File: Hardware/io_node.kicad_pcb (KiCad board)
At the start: 2 copper layers, 50 x 100 mm, 18 parts, among them U1 STM32F405RGT6, Y1 8 MHz

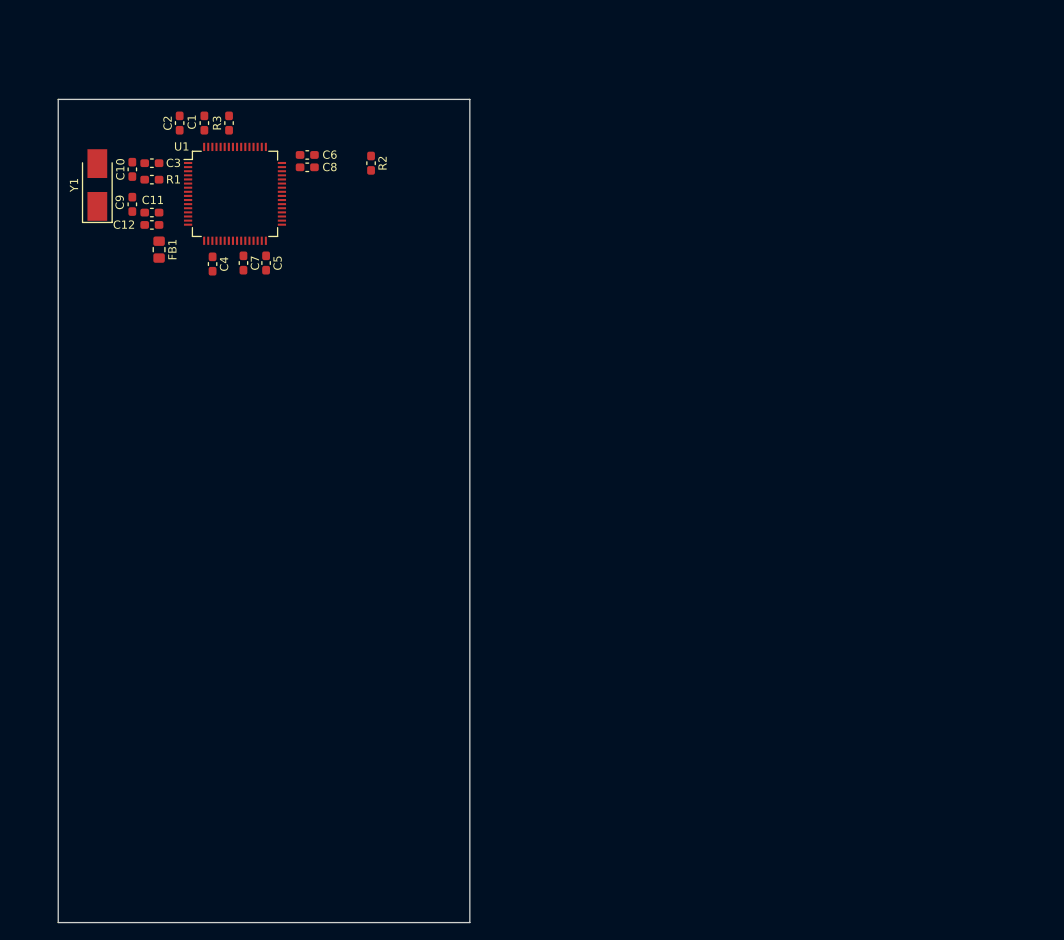
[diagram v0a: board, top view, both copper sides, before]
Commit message: Add in and output drivers
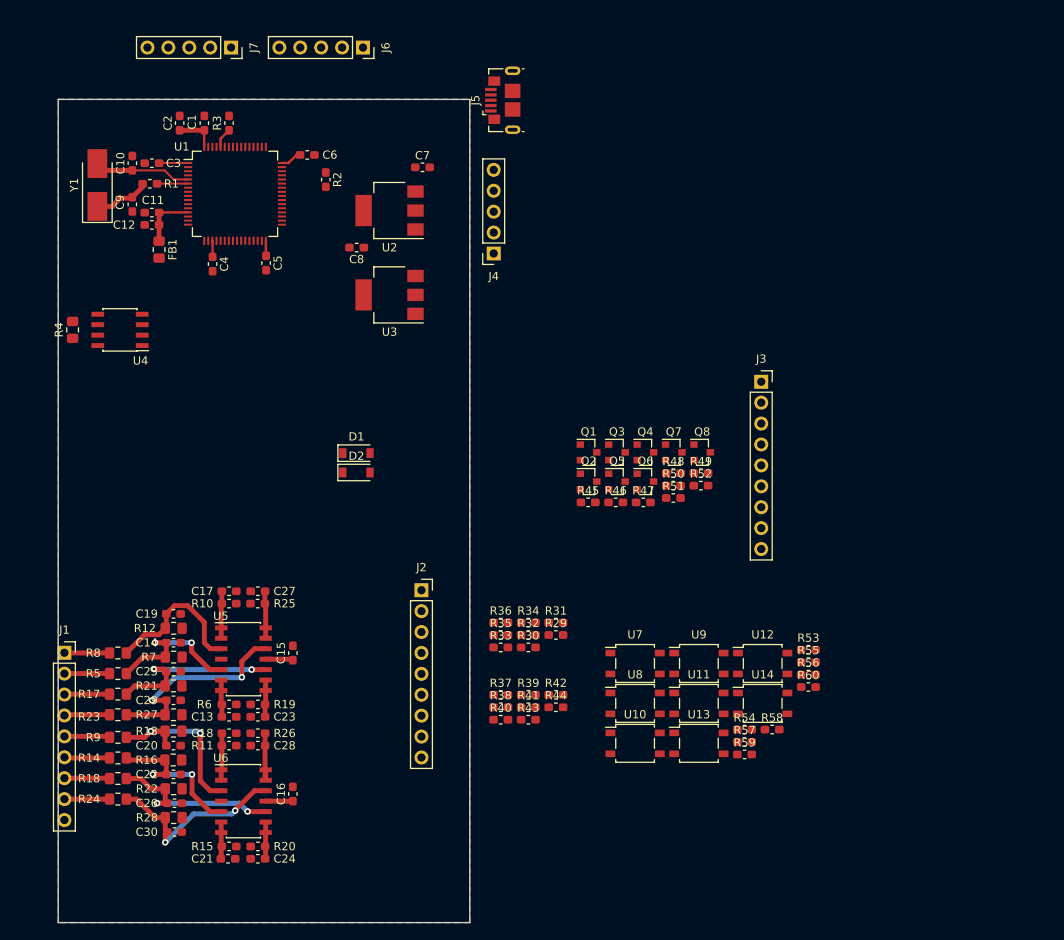
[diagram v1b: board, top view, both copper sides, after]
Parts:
- added C13: 1NF, Capacitor_SMD:C_0603_1608Metric_Pad1.05x0.95mm_HandSolder, F.Cu at (70.8, 100.0)
- added C14: 100NF, Capacitor_SMD:C_0603_1608Metric_Pad1.05x0.95mm_HandSolder, F.Cu at (64.0, 91.0)
- added C15: 100NF, Capacitor_SMD:C_0603_1608Metric_Pad1.05x0.95mm_HandSolder, F.Cu at (78.5, 92.2)
- added C16: 100NF, Capacitor_SMD:C_0603_1608Metric_Pad1.05x0.95mm_HandSolder, F.Cu at (78.5, 109.4)
- added C17: 1NF, Capacitor_SMD:C_0603_1608Metric_Pad1.05x0.95mm_HandSolder, F.Cu at (70.8, 84.8)
- added C18: 1NF, Capacitor_SMD:C_0603_1608Metric_Pad1.05x0.95mm_HandSolder, F.Cu at (70.8, 102.0)
- added C19: 100NF, Capacitor_SMD:C_0603_1608Metric_Pad1.05x0.95mm_HandSolder, F.Cu at (64.0, 87.5)
- added C20: 100NF, Capacitor_SMD:C_0603_1608Metric_Pad1.05x0.95mm_HandSolder, F.Cu at (64.0, 103.5)
- added C21: 1NF, Capacitor_SMD:C_0603_1608Metric_Pad1.05x0.95mm_HandSolder, F.Cu at (70.6, 117.2)
- added C22: 100NF, Capacitor_SMD:C_0603_1608Metric_Pad1.05x0.95mm_HandSolder, F.Cu at (64.0, 107.0)
- added C23: 1NF, Capacitor_SMD:C_0603_1608Metric_Pad1.05x0.95mm_HandSolder, F.Cu at (74.2, 100.0)
- added C24: 1NF, Capacitor_SMD:C_0603_1608Metric_Pad1.05x0.95mm_HandSolder, F.Cu at (74.2, 117.2)
- added C25: 100NF, Capacitor_SMD:C_0603_1608Metric_Pad1.05x0.95mm_HandSolder, F.Cu at (64.0, 94.5)
- added C26: 100NF, Capacitor_SMD:C_0603_1608Metric_Pad1.05x0.95mm_HandSolder, F.Cu at (64.1, 110.5)
- added C27: 1NF, Capacitor_SMD:C_0603_1608Metric_Pad1.05x0.95mm_HandSolder, F.Cu at (74.2, 84.8)
- added C28: 1NF, Capacitor_SMD:C_0603_1608Metric_Pad1.05x0.95mm_HandSolder, F.Cu at (74.2, 103.5)
- added C29: 100NF, Capacitor_SMD:C_0603_1608Metric_Pad1.05x0.95mm_HandSolder, F.Cu at (64.0, 98.0)
- added C30: 100NF, Capacitor_SMD:C_0603_1608Metric_Pad1.05x0.95mm_HandSolder, F.Cu at (64.1, 114.0)
- added D1: B5819W, Diode_SMD:D_SOD-123, F.Cu at (86.2, 68.0)
- added D2: B5819W, Diode_SMD:D_SOD-123, F.Cu at (86.2, 70.3)
- added J1: Conn_01x09, Connector_PinSocket_2.54mm:PinSocket_1x09_P2.54mm_Vertical, F.Cu at (50.8, 92.2)
- added J2: Conn_01x09, Connector_PinSocket_2.54mm:PinSocket_1x09_P2.54mm_Vertical, F.Cu at (94.1, 84.6)
- added J3: Conn_01x09, Connector_PinSocket_2.54mm:PinSocket_1x09_P2.54mm_Vertical, F.Cu at (135.4, 59.3)
- added J4: Conn_01x05, Connector_PinSocket_2.54mm:PinSocket_1x05_P2.54mm_Vertical, F.Cu at (102.9, 43.7)
- added J5: USB_B_Micro, Connector_USB:USB_Micro-B_GCT_USB3076-30-A, F.Cu at (104.0, 25.1)
- added J6: Conn_01x05, Connector_PinSocket_2.54mm:PinSocket_1x05_P2.54mm_Vertical, F.Cu at (87.0, 18.7)
- added J7: Conn_01x05, Connector_PinSocket_2.54mm:PinSocket_1x05_P2.54mm_Vertical, F.Cu at (71.0, 18.7)
- added Q1: 2N7002, Package_TO_SOT_SMD:SOT-23, F.Cu at (114.4, 67.9)
- added Q2: 2N7002, Package_TO_SOT_SMD:SOT-23, F.Cu at (114.4, 71.4)
- added Q3: 2N7002, Package_TO_SOT_SMD:SOT-23, F.Cu at (117.9, 67.9)
- added Q4: 2N7002, Package_TO_SOT_SMD:SOT-23, F.Cu at (121.3, 67.9)
- added Q5: 2N7002, Package_TO_SOT_SMD:SOT-23, F.Cu at (117.9, 71.4)
- added Q6: 2N7002, Package_TO_SOT_SMD:SOT-23, F.Cu at (121.3, 71.4)
- added Q7: 2N7002, Package_TO_SOT_SMD:SOT-23, F.Cu at (124.8, 67.9)
- added Q8: 2N7002, Package_TO_SOT_SMD:SOT-23, F.Cu at (128.2, 67.9)
- added R10: 10K, Resistor_SMD:R_0603_1608Metric_Pad1.05x0.95mm_HandSolder, F.Cu at (70.8, 86.2)
- added R11: 10K, Resistor_SMD:R_0603_1608Metric_Pad1.05x0.95mm_HandSolder, F.Cu at (70.8, 103.5)
- added R12: 10K, Resistor_SMD:R_0805_2012Metric_Pad1.15x1.40mm_HandSolder, F.Cu at (64.0, 89.2)
- added R13: 10K, Resistor_SMD:R_0805_2012Metric_Pad1.15x1.40mm_HandSolder, F.Cu at (64.0, 101.8)
- added R14: 150K, Resistor_SMD:R_0805_2012Metric_Pad1.15x1.40mm_HandSolder, F.Cu at (57.2, 105.0)
- added R15: 10K, Resistor_SMD:R_0603_1608Metric_Pad1.05x0.95mm_HandSolder, F.Cu at (70.8, 115.8)
- added R16: 10K, Resistor_SMD:R_0805_2012Metric_Pad1.15x1.40mm_HandSolder, F.Cu at (64.0, 105.2)
- added R17: 150K, Resistor_SMD:R_0805_2012Metric_Pad1.15x1.40mm_HandSolder, F.Cu at (57.2, 97.2)
- added R18: 150K, Resistor_SMD:R_0805_2012Metric_Pad1.15x1.40mm_HandSolder, F.Cu at (57.2, 107.5)
- added R19: 10K, Resistor_SMD:R_0603_1608Metric_Pad1.05x0.95mm_HandSolder, F.Cu at (74.2, 98.5)
- added R20: 10K, Resistor_SMD:R_0603_1608Metric_Pad1.05x0.95mm_HandSolder, F.Cu at (74.2, 115.8)
- added R21: 10K, Resistor_SMD:R_0805_2012Metric_Pad1.15x1.40mm_HandSolder, F.Cu at (64.0, 96.2)
- added R22: 10K, Resistor_SMD:R_0805_2012Metric_Pad1.15x1.40mm_HandSolder, F.Cu at (64.0, 108.8)
- added R23: 150K, Resistor_SMD:R_0805_2012Metric_Pad1.15x1.40mm_HandSolder, F.Cu at (57.2, 99.8)
- added R24: 150K, Resistor_SMD:R_0805_2012Metric_Pad1.15x1.40mm_HandSolder, F.Cu at (57.2, 110.0)
- added R25: 10K, Resistor_SMD:R_0603_1608Metric_Pad1.05x0.95mm_HandSolder, F.Cu at (74.2, 86.2)
- added R26: 10K, Resistor_SMD:R_0603_1608Metric_Pad1.05x0.95mm_HandSolder, F.Cu at (74.2, 102.0)
- added R27: 10K, Resistor_SMD:R_0805_2012Metric_Pad1.15x1.40mm_HandSolder, F.Cu at (64.0, 99.8)
- added R28: 10K, Resistor_SMD:R_0805_2012Metric_Pad1.15x1.40mm_HandSolder, F.Cu at (64.0, 112.2)
- added R29: 10K, Resistor_SMD:R_0603_1608Metric_Pad1.05x0.95mm_HandSolder, F.Cu at (110.5, 90.1)
- added R30: 10K, Resistor_SMD:R_0603_1608Metric_Pad1.05x0.95mm_HandSolder, F.Cu at (107.1, 91.6)
- added R31: 470R, Resistor_SMD:R_0603_1608Metric_Pad1.05x0.95mm_HandSolder, F.Cu at (110.5, 88.6)
- added R32: 470R, Resistor_SMD:R_0603_1608Metric_Pad1.05x0.95mm_HandSolder, F.Cu at (107.1, 90.1)
- added R33: 10K, Resistor_SMD:R_0603_1608Metric_Pad1.05x0.95mm_HandSolder, F.Cu at (103.8, 91.6)
- added R34: 10K, Resistor_SMD:R_0603_1608Metric_Pad1.05x0.95mm_HandSolder, F.Cu at (107.1, 88.6)
- added R35: 470R, Resistor_SMD:R_0603_1608Metric_Pad1.05x0.95mm_HandSolder, F.Cu at (103.8, 90.1)
- added R36: 470R, Resistor_SMD:R_0603_1608Metric_Pad1.05x0.95mm_HandSolder, F.Cu at (103.8, 88.6)
- added R37: 1K, Resistor_SMD:R_0603_1608Metric_Pad1.05x0.95mm_HandSolder, F.Cu at (103.8, 97.3)
- added R38: 10K, Resistor_SMD:R_0603_1608Metric_Pad1.05x0.95mm_HandSolder, F.Cu at (103.8, 98.8)
- added R39: 1K, Resistor_SMD:R_0603_1608Metric_Pad1.05x0.95mm_HandSolder, F.Cu at (107.1, 97.3)
- added R4: 120R, Resistor_SMD:R_0805_2012Metric_Pad1.15x1.40mm_HandSolder, F.Cu at (51.8, 53.0)
- added R40: 10K, Resistor_SMD:R_0603_1608Metric_Pad1.05x0.95mm_HandSolder, F.Cu at (103.8, 100.4)
- added R41: 1K, Resistor_SMD:R_0603_1608Metric_Pad1.05x0.95mm_HandSolder, F.Cu at (107.1, 98.8)
- added R42: 1K, Resistor_SMD:R_0603_1608Metric_Pad1.05x0.95mm_HandSolder, F.Cu at (110.5, 97.3)
- added R43: 10K, Resistor_SMD:R_0603_1608Metric_Pad1.05x0.95mm_HandSolder, F.Cu at (107.1, 100.4)
- added R44: 10K, Resistor_SMD:R_0603_1608Metric_Pad1.05x0.95mm_HandSolder, F.Cu at (110.5, 98.8)
- added R45: 1K, Resistor_SMD:R_0603_1608Metric_Pad1.05x0.95mm_HandSolder, F.Cu at (114.4, 74.0)
- added R46: 1K, Resistor_SMD:R_0603_1608Metric_Pad1.05x0.95mm_HandSolder, F.Cu at (117.7, 74.0)
- added R47: 10K, Resistor_SMD:R_0603_1608Metric_Pad1.05x0.95mm_HandSolder, F.Cu at (121.1, 74.0)
- added R48: 10K, Resistor_SMD:R_0603_1608Metric_Pad1.05x0.95mm_HandSolder, F.Cu at (124.7, 70.4)
- added R49: 1K, Resistor_SMD:R_0603_1608Metric_Pad1.05x0.95mm_HandSolder, F.Cu at (128.1, 70.4)
- added R5: 150K, Resistor_SMD:R_0805_2012Metric_Pad1.15x1.40mm_HandSolder, F.Cu at (57.2, 94.8)
- added R50: 1K, Resistor_SMD:R_0603_1608Metric_Pad1.05x0.95mm_HandSolder, F.Cu at (124.7, 71.9)
- added R51: 10K, Resistor_SMD:R_0603_1608Metric_Pad1.05x0.95mm_HandSolder, F.Cu at (124.7, 73.4)
- added R52: 10K, Resistor_SMD:R_0603_1608Metric_Pad1.05x0.95mm_HandSolder, F.Cu at (128.1, 71.9)
- added R53: 10K, Resistor_SMD:R_0603_1608Metric_Pad1.05x0.95mm_HandSolder, F.Cu at (141.1, 91.9)
- added R54: 10K, Resistor_SMD:R_0603_1608Metric_Pad1.05x0.95mm_HandSolder, F.Cu at (133.4, 101.6)
- added R55: 470R, Resistor_SMD:R_0603_1608Metric_Pad1.05x0.95mm_HandSolder, F.Cu at (141.1, 93.4)
- added R56: 470R, Resistor_SMD:R_0603_1608Metric_Pad1.05x0.95mm_HandSolder, F.Cu at (141.1, 94.9)
- added R57: 10K, Resistor_SMD:R_0603_1608Metric_Pad1.05x0.95mm_HandSolder, F.Cu at (133.4, 103.1)
- added R58: 10K, Resistor_SMD:R_0603_1608Metric_Pad1.05x0.95mm_HandSolder, F.Cu at (136.7, 101.6)
- added R59: 470R, Resistor_SMD:R_0603_1608Metric_Pad1.05x0.95mm_HandSolder, F.Cu at (133.4, 104.6)
- added R6: 10K, Resistor_SMD:R_0603_1608Metric_Pad1.05x0.95mm_HandSolder, F.Cu at (70.8, 98.5)
- added R60: 470R, Resistor_SMD:R_0603_1608Metric_Pad1.05x0.95mm_HandSolder, F.Cu at (141.1, 96.4)
- added R7: 10K, Resistor_SMD:R_0805_2012Metric_Pad1.15x1.40mm_HandSolder, F.Cu at (64.0, 92.8)
- added R8: 150K, Resistor_SMD:R_0805_2012Metric_Pad1.15x1.40mm_HandSolder, F.Cu at (57.2, 92.2)
- added R9: 150K, Resistor_SMD:R_0805_2012Metric_Pad1.15x1.40mm_HandSolder, F.Cu at (57.2, 102.5)
- added U10: EL357N-G, Package_SO:SO-4_4.4x4.3mm_P2.54mm, F.Cu at (120.1, 103.2)
- added U11: EL357N-G, Package_SO:SO-4_4.4x4.3mm_P2.54mm, F.Cu at (127.8, 98.4)
- added U12: EL357N-G, Package_SO:SO-4_4.4x4.3mm_P2.54mm, F.Cu at (135.6, 93.5)
- added U13: EL357N-G, Package_SO:SO-4_4.4x4.3mm_P2.54mm, F.Cu at (127.8, 103.2)
- added U14: EL357N-G, Package_SO:SO-4_4.4x4.3mm_P2.54mm, F.Cu at (135.6, 98.4)
- added U2: AMS1117-5.0, Package_TO_SOT_SMD:SOT-223-3_TabPin2, F.Cu at (90.2, 38.5)
- added U3: AMS1117-3.3, Package_TO_SOT_SMD:SOT-223-3_TabPin2, F.Cu at (90.2, 48.8)
- added U4: SP3485EN, Package_SO:SOIC-8_3.9x4.9mm_P1.27mm, F.Cu at (57.5, 53.0)
- added U5: TLV274CPWR, Package_SO:SOIC-14_3.9x8.7mm_P1.27mm, F.Cu at (72.5, 93.0)
- added U6: TLV274CPWR, Package_SO:SOIC-14_3.9x8.7mm_P1.27mm, F.Cu at (72.5, 110.2)
- added U7: EL357N-G, Package_SO:SO-4_4.4x4.3mm_P2.54mm, F.Cu at (120.1, 93.5)
- added U8: EL357N-G, Package_SO:SO-4_4.4x4.3mm_P2.54mm, F.Cu at (120.1, 98.4)
- added U9: EL357N-G, Package_SO:SO-4_4.4x4.3mm_P2.54mm, F.Cu at (127.8, 93.5)
- C7: value 2_2UF -> 4_7UF
- C8: value 2_2UF -> 100NF
- U1: value STM32F405RGT6 -> STM32F103RBT6
- moved C7 24.7 mm to (94.2, 33.2), turned to 0 degrees
- moved C8 11.4 mm to (86.2, 43.0), turned to 180 degrees
- moved R2 5.85 mm to (82.5, 34.8)
- moved C10 0.75 mm to (59.0, 32.8)
- moved R1 0.56 mm to (61.1, 35.2)
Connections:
- net Net-(R3-Pad1) renamed /BOOT0
- net Net-(U1-Pad46) renamed /SWDIO
- net Net-(U1-Pad49) renamed /SWCLK
- C7 pad 1: Net-(C7-Pad1) -> V_IN
- C8 pad 1: Net-(C8-Pad1) -> +5V
- R1 pad 2: Net-(C10-Pad1) -> Net-(C9-Pad1)
- U1 pad 10: Net-(U1-Pad10) -> /IN_2
- U1 pad 11: Net-(U1-Pad11) -> /IN_3
- U1 pad 14: Net-(U1-Pad14) -> /ADC_IN0
- U1 pad 15: Net-(U1-Pad15) -> /ADC_IN1
- U1 pad 16: Net-(U1-Pad16) -> /USART2_TX
- U1 pad 17: Net-(U1-Pad17) -> /USART2_RX
- U1 pad 2: Net-(U1-Pad2) -> /OUT_5
- U1 pad 20: Net-(U1-Pad20) -> /USART2_DE
- U1 pad 21: Net-(U1-Pad21) -> /ADC_IN5
- U1 pad 22: Net-(U1-Pad22) -> /ADC_IN6
- U1 pad 23: Net-(U1-Pad23) -> /ADC_IN7
- U1 pad 24: Net-(U1-Pad24) -> /IN_4
- U1 pad 25: Net-(U1-Pad25) -> /IN_5
- U1 pad 26: Net-(U1-Pad26) -> /ADC_IN8
- U1 pad 27: Net-(U1-Pad27) -> /ADC_IN9
- U1 pad 28: Net-(U1-Pad28) -> /SPI1_CS
- U1 pad 3: Net-(U1-Pad3) -> /OUT_6
- U1 pad 31: Net-(C7-Pad1) -> GND
- U1 pad 37: Net-(U1-Pad37) -> /TIM3_CH1
- U1 pad 38: Net-(U1-Pad38) -> /TIM3_CH2
- U1 pad 39: Net-(U1-Pad39) -> /TIM3_CH3
- U1 pad 4: Net-(U1-Pad4) -> /OUT_7
- U1 pad 40: Net-(U1-Pad40) -> /TIM3_CH4
- U1 pad 42: Net-(U1-Pad42) -> /USART1_TX
- U1 pad 43: Net-(U1-Pad43) -> /USART1_RX
- U1 pad 44: Net-(U1-Pad44) -> /USB_DM
- U1 pad 45: Net-(U1-Pad45) -> /USB_DP
- U1 pad 47: Net-(C8-Pad1) -> GND
- U1 pad 5: Net-(R1-Pad1) -> Net-(C10-Pad1)
- U1 pad 51: Net-(U1-Pad51) -> /IN_0
- U1 pad 53: Net-(U1-Pad53) -> /OUT_4
- U1 pad 55: Net-(U1-Pad55) -> /SPI1_SCK
- U1 pad 56: Net-(U1-Pad56) -> /SPI1_MISO
- U1 pad 57: Net-(U1-Pad57) -> /SPI1_MOSI
- U1 pad 58: Net-(U1-Pad58) -> /IN_6
- U1 pad 59: Net-(U1-Pad59) -> /IN_7
- U1 pad 6: Net-(C9-Pad1) -> Net-(R1-Pad1)
- U1 pad 61: Net-(U1-Pad61) -> /I2C1_SCL
- U1 pad 62: Net-(U1-Pad62) -> /I2C1_SDA
- U1 pad 8: Net-(U1-Pad8) -> /ADC_IN10
- U1 pad 9: Net-(U1-Pad9) -> /IN_1
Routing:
- net Net-(C29-Pad1): track 0.00 -> 25.8 mm, vias 0 -> 2
- net Net-(C30-Pad1): track 0.00 -> 23.7 mm, vias 0 -> 2
- net Net-(C25-Pad1): track 0.00 -> 22.3 mm, vias 0 -> 2
- net Net-(C26-Pad1): track 0.00 -> 22.0 mm, vias 0 -> 2
- net Net-(C20-Pad1): track 0.00 -> 21.8 mm, vias 0 -> 2
- net Net-(C22-Pad1): track 0.00 -> 19.8 mm, vias 0 -> 2
- net Net-(C14-Pad1): track 0.00 -> 18.8 mm, vias 0 -> 2
- net Net-(C19-Pad1): track 0.00 -> 18.5 mm
- net +3V3: track 0.00 -> 15.0 mm
- net +3.3VA: track 0.00 -> 13.7 mm
- net Net-(C10-Pad1): track 0.00 -> 11.8 mm
- net Net-(C9-Pad1): track 0.00 -> 6.86 mm
- net /ADC_IN10: track 0.00 -> 6.49 mm
- net /ADC_IN6: track 0.00 -> 5.76 mm
- net /ADC_IN7: track 0.00 -> 5.74 mm
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- added copper zone on B.Cu, net GND
- added copper zone on F.Cu, net GND

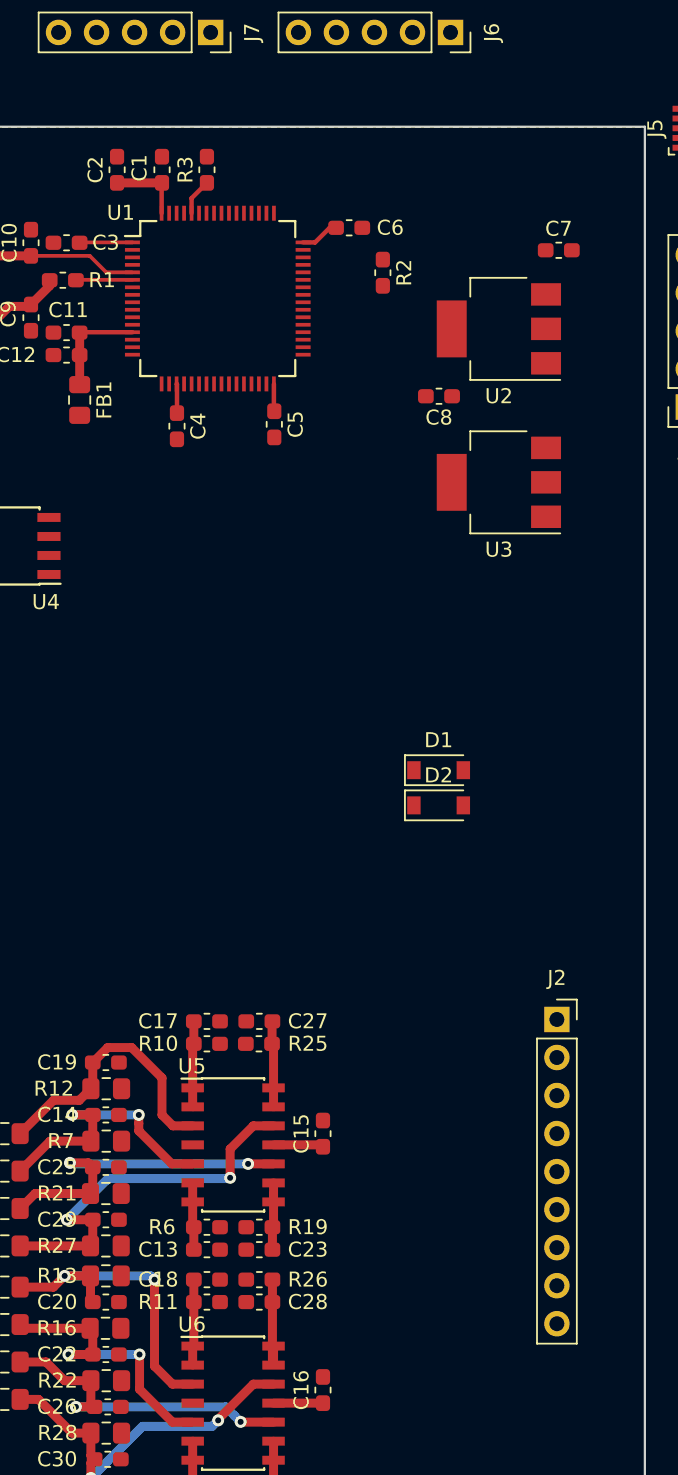
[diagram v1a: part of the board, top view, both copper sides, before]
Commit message: Add USB protection
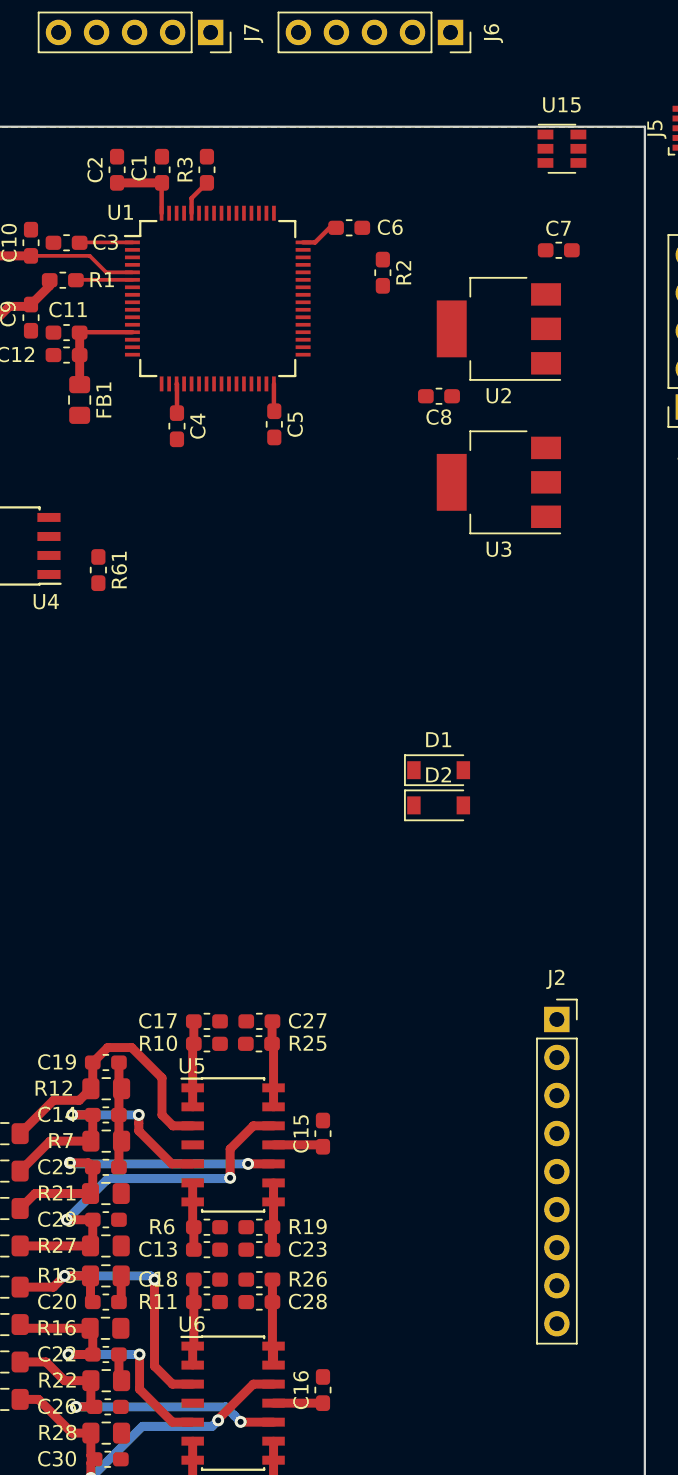
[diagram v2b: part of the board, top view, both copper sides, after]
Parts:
- added R61: 10K, Resistor_SMD:R_0603_1608Metric_Pad1.05x0.95mm_HandSolder, F.Cu at (63.5, 54.6)
- added U15: USBLC6-2SC6, Package_TO_SOT_SMD:SOT-23-6, F.Cu at (94.5, 26.5)
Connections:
- net Net-(D1-Pad2) renamed VBUS
- J5 pad 2: /USB_DM -> /USB_CONN_DM
- J5 pad 3: /USB_DP -> /USB_CONN_DP
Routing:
- net GND: track 0.00 -> 10.6 mm

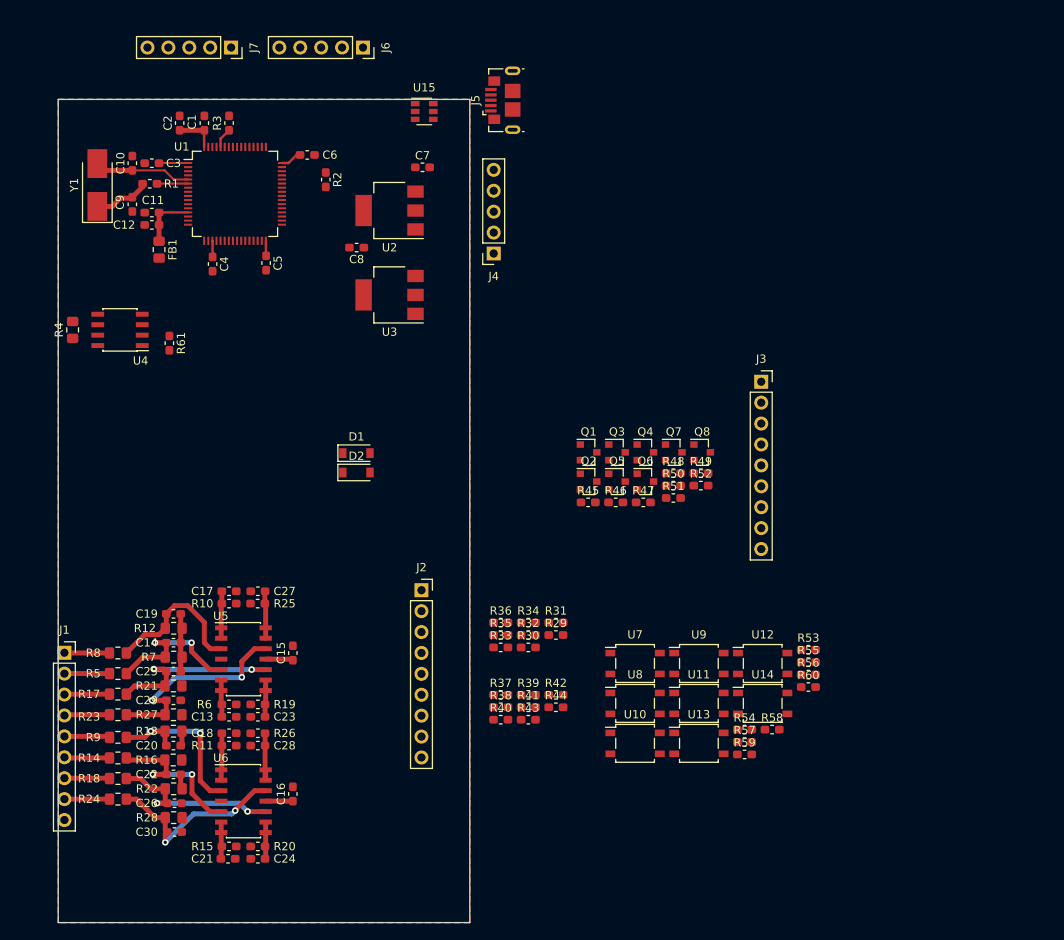
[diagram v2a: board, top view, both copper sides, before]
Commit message: Add power connector
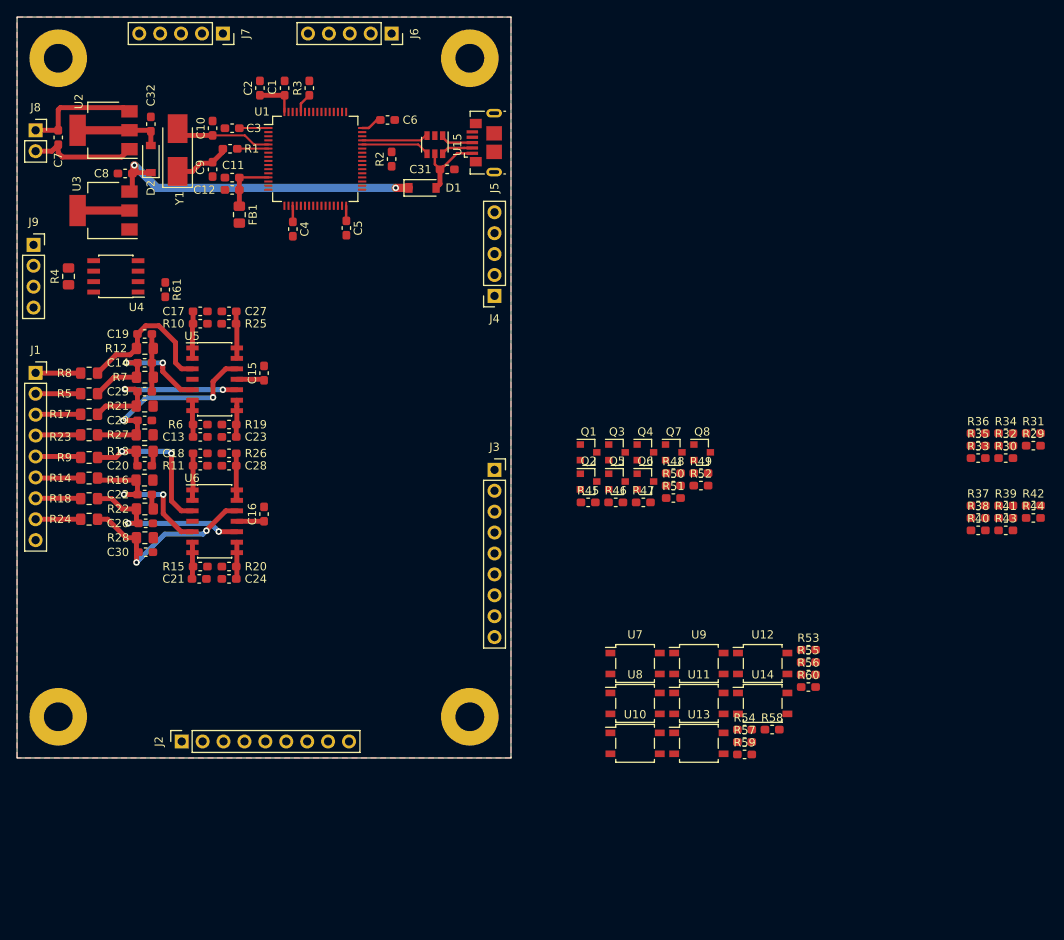
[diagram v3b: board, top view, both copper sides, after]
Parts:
- added C31: 100NF, Capacitor_SMD:C_0603_1608Metric_Pad1.05x0.95mm_HandSolder, F.Cu at (97.2, 33.5)
- added C32: 100NF, Capacitor_SMD:C_0603_1608Metric_Pad1.05x0.95mm_HandSolder, F.Cu at (61.2, 28.0)
- added H1: MountingHole_Pad, MountingHole:MountingHole_3.5mm_Pad, F.Cu at (50.0, 20.0)
- added H2: MountingHole_Pad, MountingHole:MountingHole_3.5mm_Pad, F.Cu at (50.0, 100.0)
- added H3: MountingHole_Pad, MountingHole:MountingHole_3.5mm_Pad, F.Cu at (100.0, 20.0)
- added H4: MountingHole_Pad, MountingHole:MountingHole_3.5mm_Pad, F.Cu at (100.0, 100.0)
- added J8: Conn_01x02, Connector_PinSocket_2.54mm:PinSocket_1x02_P2.54mm_Vertical, F.Cu at (47.2, 28.8)
- added J9: Conn_01x04, Connector_PinSocket_2.54mm:PinSocket_1x04_P2.54mm_Vertical, F.Cu at (47.0, 42.7)
- moved R29 62.4 mm to (168.5, 67.1)
- moved R31 62.4 mm to (168.5, 65.6)
- moved R42 62.4 mm to (168.5, 74.3)
- moved R44 62.4 mm to (168.5, 75.8)
- moved R33 62.4 mm to (161.8, 68.6)
- moved R35 62.4 mm to (161.8, 67.1)
- moved R36 62.4 mm to (161.8, 65.6)
- moved R37 62.4 mm to (161.8, 74.3)
- moved R38 62.4 mm to (161.8, 75.8)
- moved R40 62.4 mm to (161.8, 77.4)
- moved R30 62.4 mm to (165.1, 68.6)
- moved R32 62.4 mm to (165.1, 67.1)
- moved R34 62.4 mm to (165.1, 65.6)
- moved R39 62.4 mm to (165.1, 74.3)
- moved R41 62.4 mm to (165.1, 75.8)
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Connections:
- net /USB_DM renamed /USB_N
- net /USB_DP renamed /USB_P
- net V_IN renamed +12V
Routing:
- net +5V: track 0.00 -> 40.2 mm, vias 0 -> 2
- net +12V: track 0.00 -> 14.2 mm
- net GND: track 10.6 -> 24.0 mm
- net Net-(C32-Pad1): track 0.00 -> 10.7 mm
- net VBUS: track 0.00 -> 9.34 mm
- net /USB_N: track 0.00 -> 8.37 mm
- net /USB_P: track 0.00 -> 8.11 mm
- net +3V3: track 15.0 -> 21.3 mm
- net /USB_CONN_DP: track 0.00 -> 4.07 mm
- net /USB_CONN_DM: track 0.00 -> 3.92 mm
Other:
- board size 50 x 100 mm -> 60 x 90 mm
